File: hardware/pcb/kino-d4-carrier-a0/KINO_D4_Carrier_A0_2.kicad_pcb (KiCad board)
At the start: 4 copper layers, 117 x 69.4 mm, 250 parts, among them J100 P4 JP1 - 26 pin IDC, J1000 USB4105-GF-A, J101 C6 service - 3V3 sense only, J102 3V3 I2C accessory, J1100 PROTECTED 1S PACK / NTC, J1300 POWER PUSHBUTTON, J200 XIAO ESP32-S3 Sense socket, J201 GPIO breakout - SD/strap rest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, J300 XIAO ESP32-S3 Sense socket, J301 GPIO breakout - SD/strap rest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, J400 XIAO ESP32-S3 Sense socket, J401 GPIO breakout - SD/strap rest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, J500 XIAO ESP32-S3 Sense socket, J501 GPIO breakout - SD/strap rest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, J600 POGO TEST - SENSE ONLY, J601 EXTERNAL FLASH LOGIC, J800 3V PRIMARY RTC BACKUP, J900 HAPTIC MOTOR, J901 COVER HALL SENSOR, J902 LOCAL SHUTTER, J903 REMOTE DRY CONTACT, J904 FUNCTION BUTTON, Q1000 AO4407A, Q1001 AO4407A, Q1200 AO4407A, Q1201 AO4407A, Q1202 2N7002, Q1300 2N7002, Q900 2N7002, U100 TCA9517ADGKR, U1000 STUSB4500QTR, U1100 BQ25798RQMR, U1200 TPS61288LRQQR, U1201 TPS62162DSGR, U1300 LTC2955ITS8-1, U200 TXU0304PWR, U201 TPS2553DBVR, U300 TXU0304PWR, U301 TPS2553DBVR, U400 TXU0304PWR, U401 TPS2553DBVR, U500 TXU0304PWR, U501 TPS2553DBVR, U600 TCA9539PWR, U601 SN74LVC08APWR, U700 PAC1954T-E/4MX, U701 BQ27441DRZR-G1A, U800 LSM6DSOXTR, U801 RV-3028-C7, U802 TMP117AIDRVR, U900 DRV2605LDGSR, U901 SN74LVC1G14DBVR

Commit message: feat(hardware): carrier A0.2 - U601 re-wired so every pin can leave
MB_3V3 ran under U601 along its right pin column and CAM_GLOBAL_EN
looped round both columns, walling in pins 2-3 and 10-11. C602 moves
beside VCC pin 14 (the trunk reaches it on In2), GLOBAL_EN ties its four
inputs once under the package, and CAM1_EN, CAM3_EN, CAM3_REQ and CAM4_EN
are routed: CAM3_EN down the one In2 column left between the SYS_5V
riser and camera 3's fan. handroute.py gains a place phase and duplicate
rips. 57 -> 53 open; no clearance or short errors.

Co-Authored-By: Claude Opus 5.5 <noreply@anthropic.com>
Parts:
- moved C602 8.69 mm to (121.7, 60.3), turned to 180 degrees
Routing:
- net CAM3_EN: track 3.61 -> 37.2 mm, vias 0 -> 5
- net CAM3_REQ: track 19.8 -> 48.8 mm, vias 2 -> 4
- net CAM4_EN: track 26.7 -> 37.3 mm
- net CAM1_EN: track 93.3 -> 101.2 mm, vias 5 -> 6
- net MB_3V3: track 398.2 -> 405.2 mm, vias 29 -> 31
- net CAM_GLOBAL_EN: track 38.6 -> 35.7 mm, vias 3 -> 1
- net GND: vias 155 -> 153

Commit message: feat(hardware): carrier A0.2 - expander lines along the top edge, U900 motor pair
- FN_N (In2) and COVER_N (B) from U600 along the top edge to J904 and the
  cover-sensor network, above the U601 verticals.
- U900: the MB_3V3 loop round pins 6-10 and pin 8's GND stub under the
  package walled in MOTOR_P. Pins 6 and 10 now join on In2, pin 8 takes
  the F pour, and MOTOR_P runs In2 beside MOTOR_N to J900.
- MB_3V3 to the remote chain beside J903; CAM1_EN's J600 test leg meets
  U201's EN node.
- README: the hand scripts since the Kelvin pairs.
53 -> 47 open; no clearance or short errors.

Co-Authored-By: Claude Opus 5.5 <noreply@anthropic.com>
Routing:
- net COVER_N: track 19.3 -> 120.6 mm, vias 1 -> 4
- net FN_N: track 9.96 -> 88.7 mm, vias 1 -> 3
- net MOTOR_P: track 0.00 -> 19.8 mm, vias 0 -> 2
- net MB_3V3: track 405.2 -> 422.1 mm, vias 31 -> 32
- net GND: track 81.3 -> 78.8 mm, vias 153 -> 151
- net CAM1_EN: track 101.2 -> 102.2 mm

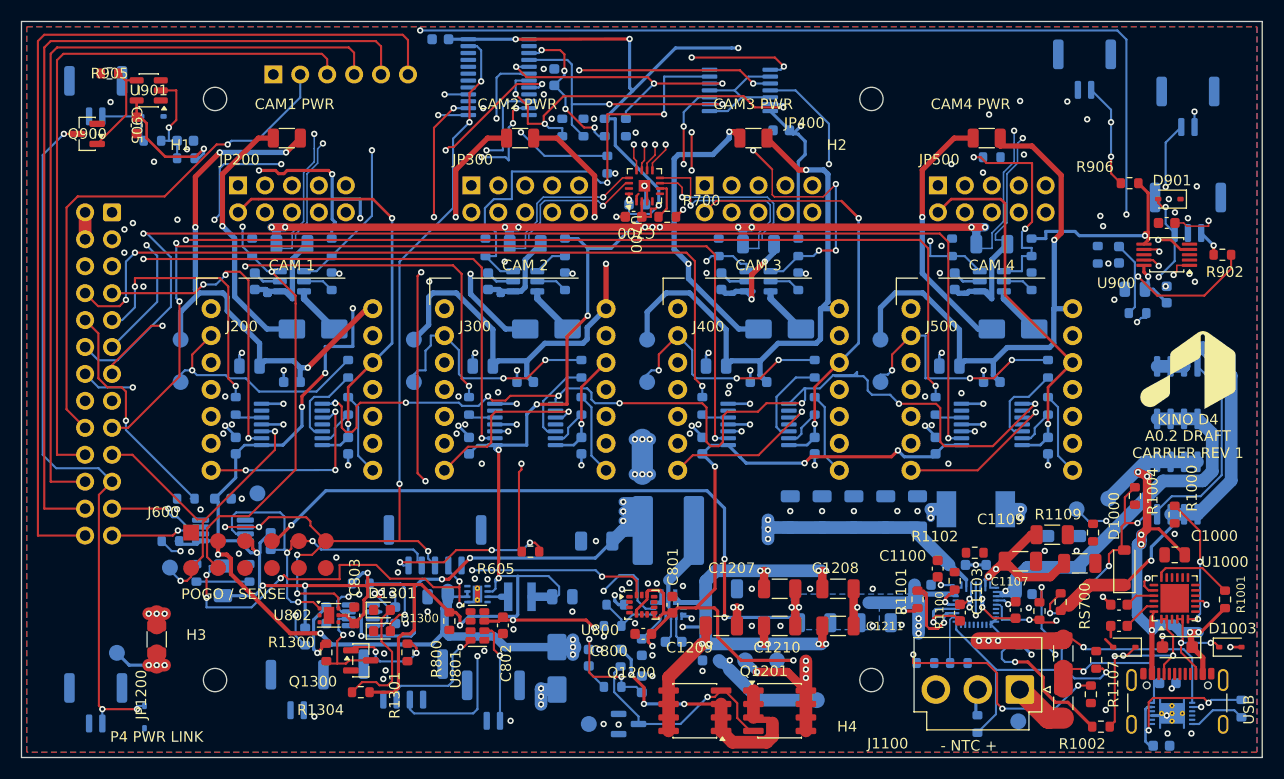
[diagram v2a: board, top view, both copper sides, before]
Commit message: feat(hardware): carrier A0.2 - expander port 1 in layout order, channel bundle
U600's port 1 GPIOs (pins 13-20) are interchangeable. North- and
south-bound lines sat interleaved, so every line leaving south crossed
one leaving north. circuit.py now maps P1.0-P1.7 to IMU_INT, RTC_INT_N,
SOFT_KILL, CHARGE_STAT_N, POWER_INT_N, FN_N, HAPTIC_EN, COVER_N (the U600
note had pin 20 as P1.3; it is P1.7). Capture, BOM, netlist, ERC (0) and
PDF are regenerated; firmware must follow the new map.

The five south-bound lines and I2C_SCL now run as one bundle between the
camera 1 and 2 sockets: F rows from U600, vias below the camera lanes,
In2 straight down, vias above the SYNC bus. POWER_INT_N's old route
round the channel goes; the CAM1_3V3 and P4_BUS_EN vias step aside.
RTC_INT_N joins R800 and U801 directly once an MB_3V3 via between them
moves. Router: the last links of RTC_INT_N, SOFT_KILL and IMU_INT.
47 -> 42 open; no clearance or short errors; parity clean.

Co-Authored-By: Claude Opus 5.5 <noreply@anthropic.com>
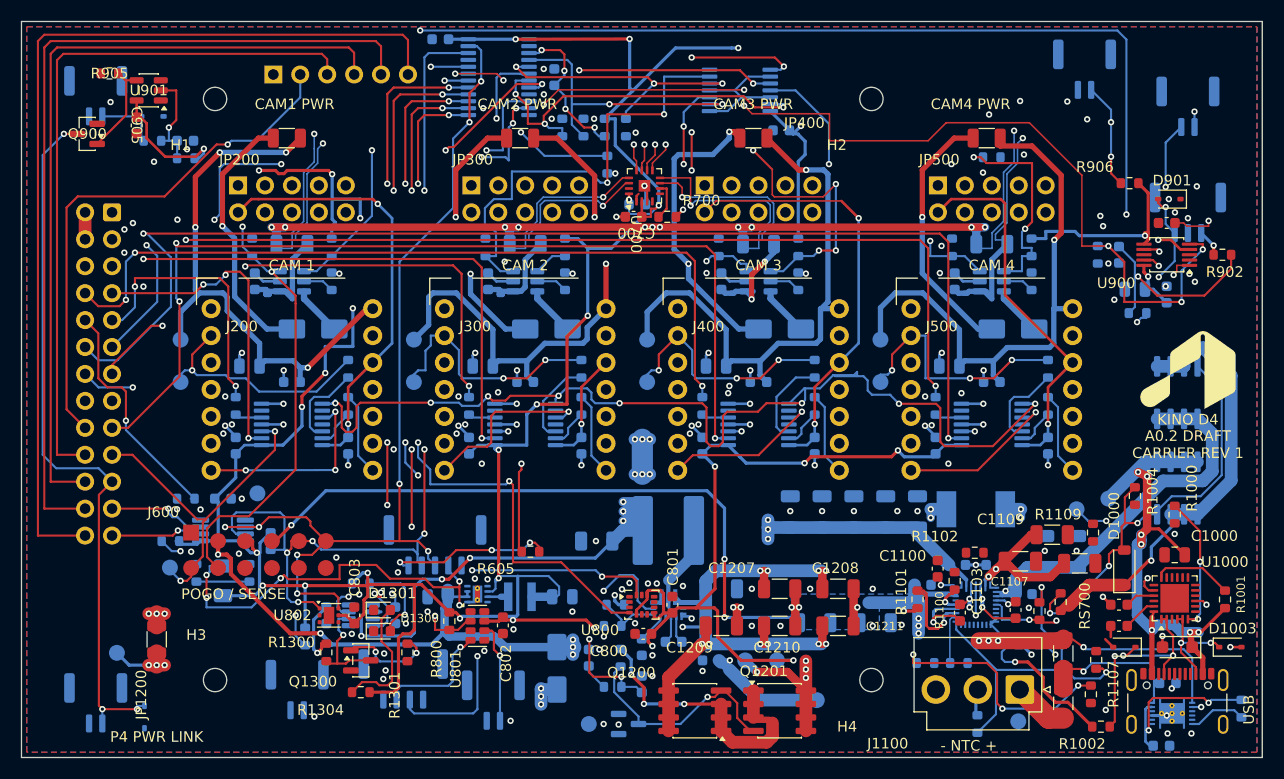
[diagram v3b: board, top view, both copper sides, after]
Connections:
- U600 pad 13: COVER_N -> IMU_INT
- U600 pad 14: POWER_INT_N -> RTC_INT_N
- U600 pad 16: FN_N -> CHARGE_STAT_N
- U600 pad 17: IMU_INT -> POWER_INT_N
- U600 pad 18: RTC_INT_N -> FN_N
- U600 pad 20: CHARGE_STAT_N -> COVER_N
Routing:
- net HAPTIC_EN: track 0.00 -> 98.2 mm, vias 0 -> 8
- net IMU_INT: track 0.00 -> 68.0 mm, vias 0 -> 4
- net SOFT_KILL: track 9.13 -> 69.0 mm, vias 2 -> 6
- net RTC_INT_N: track 0.00 -> 58.8 mm, vias 0 -> 5
- net I2C_SCL: track 35.2 -> 86.6 mm, vias 3 -> 6
- net CHARGE_STAT_N: track 0.00 -> 40.2 mm, vias 0 -> 3
- net POWER_INT_N: track 68.3 -> 73.0 mm
- net COVER_N: track 120.6 -> 116.5 mm
- net FN_N: track 88.7 -> 87.4 mm
- net MB_3V3: track 422.1 -> 421.1 mm
- net GND: vias 151 -> 150
